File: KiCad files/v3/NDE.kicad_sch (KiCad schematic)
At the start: 17 parts, among them J1 Nabíjací modul, J14 VM_Select, J2 Step-up input, J3 Step-up output, U1 LM7805_TO220

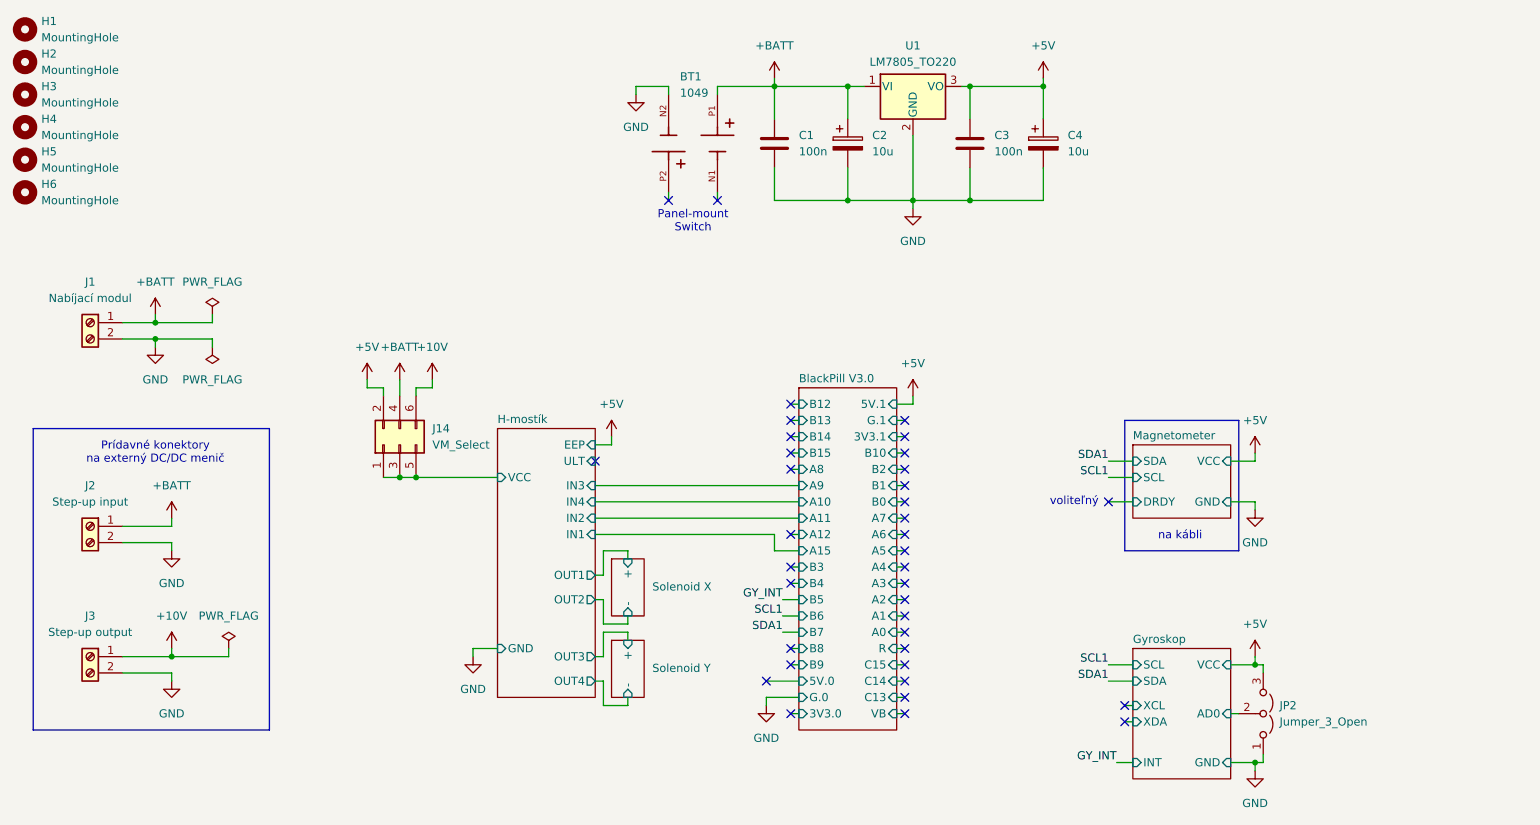
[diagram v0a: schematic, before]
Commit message: Updated schematic labeling
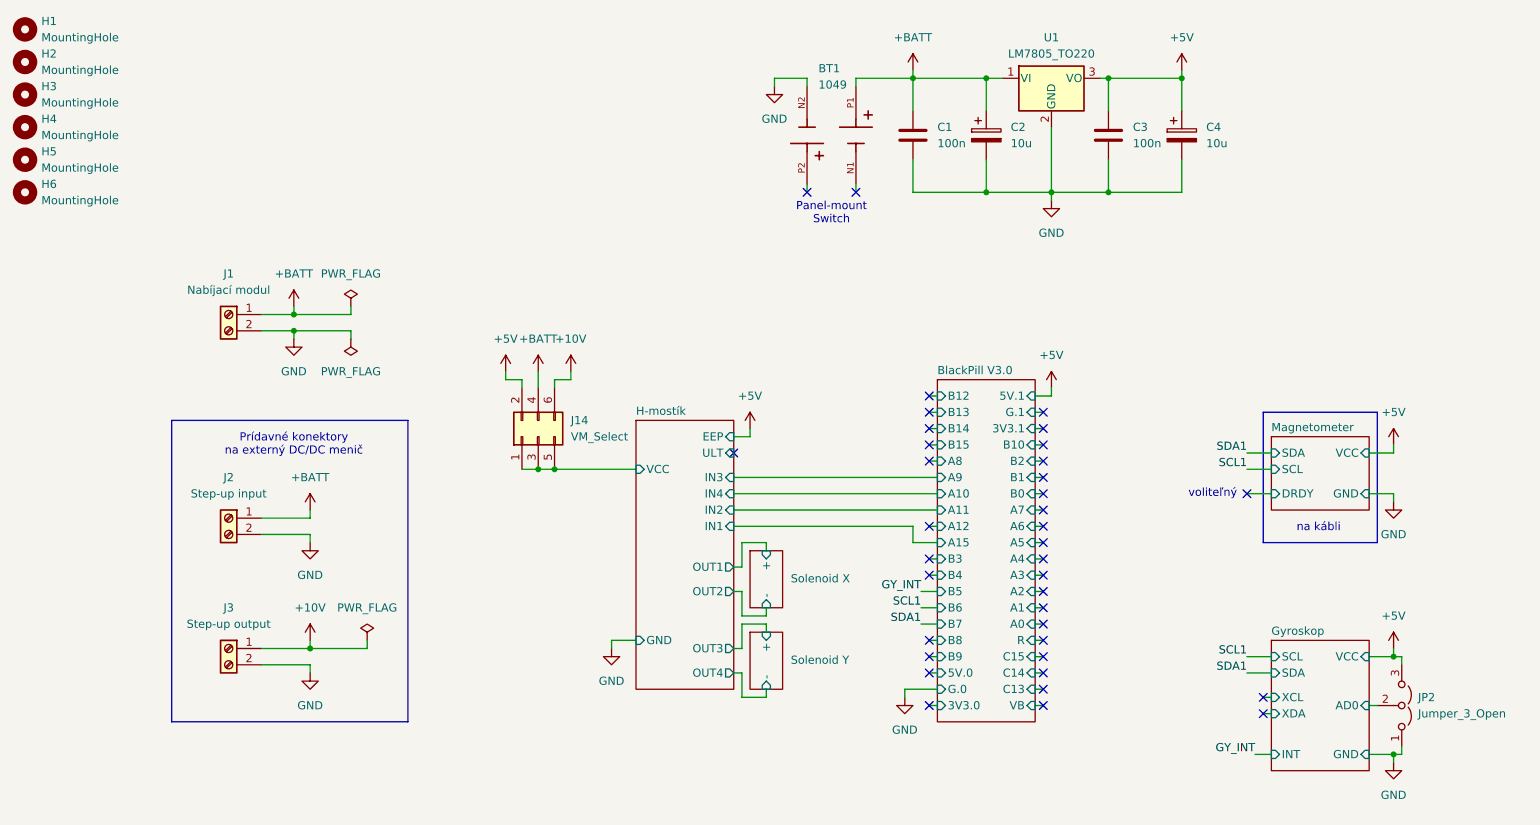
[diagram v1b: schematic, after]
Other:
- title: (none) -> Magnetorquer Control Board
- moved on the sheet: BT1, C1, C2, C3, C4, J1, J14, J2, J3, JP2, U1
